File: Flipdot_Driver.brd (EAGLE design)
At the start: 146 x 75.9 mm, 27 parts

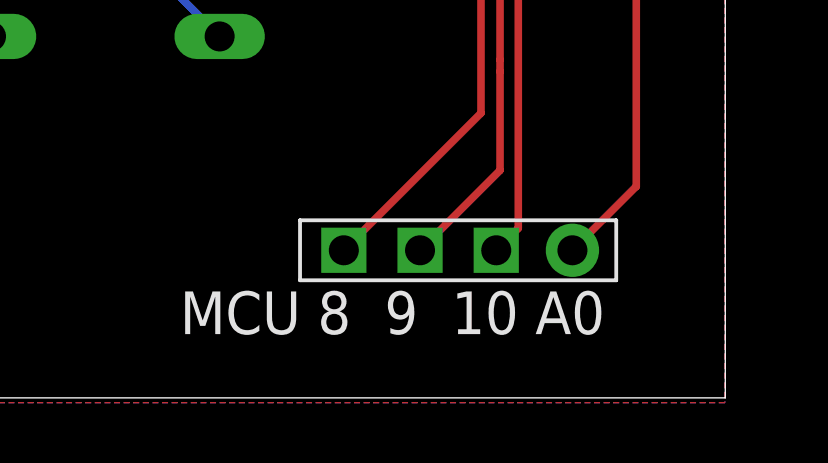
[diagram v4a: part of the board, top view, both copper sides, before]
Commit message: Remapped outputs, replaced MCU
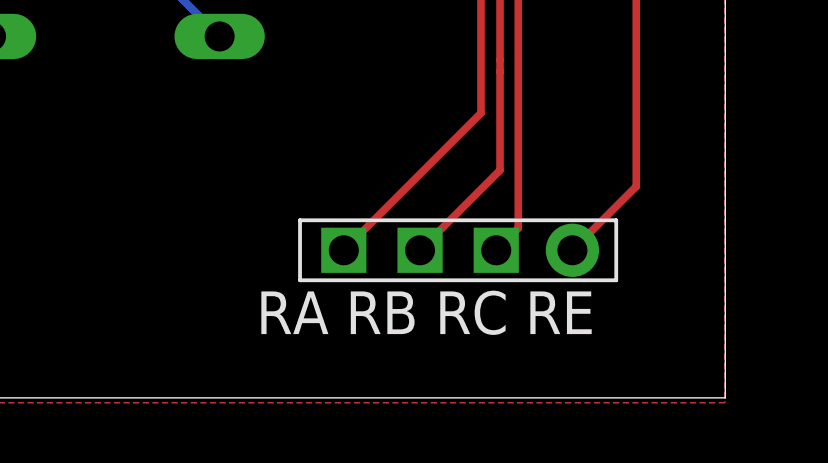
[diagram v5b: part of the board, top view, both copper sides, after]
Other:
- board text added: "A B C"
- board text added: "EA EB EC"
- board text added: "RA RB RC RE"
- board text removed: "MCU 2 3 4"
- board text removed: "MCU 5 6 7"
- board text removed: "MCU 8 9 10 A0"
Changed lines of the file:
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@@
 <?xml version="1.0" encoding="utf-8"?>
 <!DOCTYPE eagle SYSTEM "eagle.dtd">
-<eagle version="9.2.2">
+<eagle version="9.3.2">
 <drawing>
 <settings>
@@
 <wire x1="0.035" y1="76.03" x2="0.035" y2="0.16" width="0" layer="20"/>
 <text x="113.665" y="68.58" size="1.4224" layer="51">GND  5V  10V</text>
-<text x="18.161" y="2.921" size="1.4224" layer="51" rot="R90">MCU 2  3  4</text>
-<text x="2.54" y="52.07" size="1.4224" layer="51">MCU 5  6  7</text>
+<text x="13.081" y="8.001" size="1.4224" layer="51" rot="R90">A  B  C</text>
+<text x="2.159" y="51.943" size="1.4224" layer="51">EA EB EC</text>
 <text x="26.543" y="37.592" size="1.778" layer="51">The cake is a lie.</text>
-<text x="127.889" y="2.286" size="1.4224" layer="25">MCU 8  9  10 A0</text>
+<text x="130.429" y="2.286" size="1.4224" layer="25">RA RB RC RE</text>
 <text x="11.049" y="69.85" size="1.4224" layer="25">Seg. Sel.</text>
 </plain>

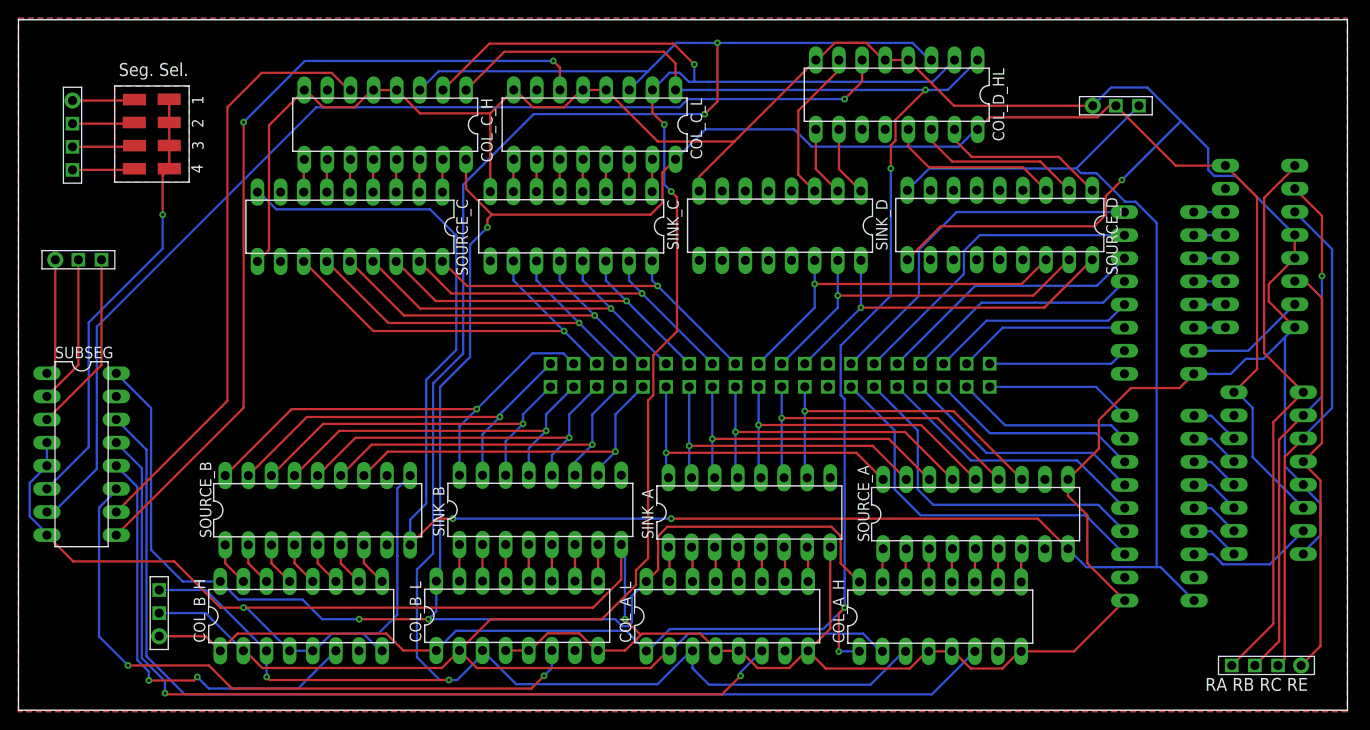
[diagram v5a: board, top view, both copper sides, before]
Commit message: Smaller PCB design
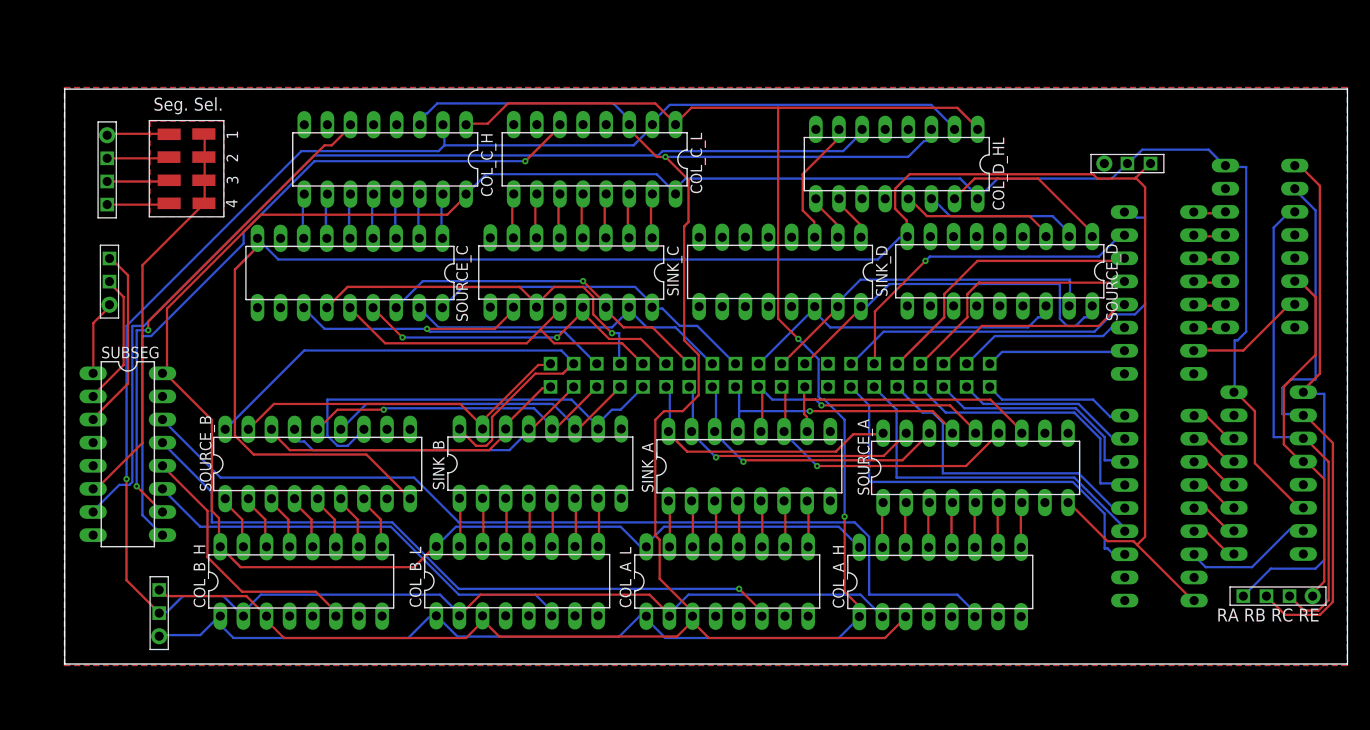
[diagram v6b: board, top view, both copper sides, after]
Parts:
- moved U$6 7.73 mm to (139.7, 12.7)
- moved COL_D_HL 7.62 mm to (96.5, 60.2)
- moved U$5 6.48 mm to (121.9, 60.2)
- moved U$10 5.39 mm to (18.5, 59.7)
- moved U$11 5.39 mm to (9.78, 60.8)
- moved SINK_A 5.08 mm to (80.3, 27.0)
- moved SINK_B 5.08 mm to (57.4, 27.3)
- moved SOURCE_B 5.08 mm to (32.9, 27.2)
- moved SUBSEG 5.08 mm to (12.0, 28.3)
- moved SINK_C 5.08 mm to (60.8, 48.3)
- moved SINK_D 5.08 mm to (83.7, 48.3)
- moved SOURCE_A 5.08 mm to (105.2, 26.8)
- moved SOURCE_C 5.08 mm to (36.5, 48.2)
- moved SOURCE_D 5.08 mm to (107.9, 48.4)
- moved U$3 4.18 mm to (10.0, 47.3), turned to 90 degrees
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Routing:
- net GND: track 519.3 -> 0.00 mm, vias 3 -> 0
- net C: track 255.4 -> 211.0 mm, vias 4 -> 1
- net 5V: track 305.1 -> 278.8 mm, vias 3 -> 0
- net N$10: track 72.0 -> 48.9 mm, vias 2 -> 0
- net N$7: track 97.6 -> 76.0 mm, vias 2 -> 1
- net N$9: track 122.1 -> 102.2 mm
- net N$8: track 48.0 -> 29.2 mm, vias 2 -> 0
- net 10V: track 229.4 -> 213.2 mm, vias 2 -> 0
- net N$12: track 91.5 -> 79.2 mm, vias 2 -> 1
- net N$11: track 65.4 -> 54.9 mm, vias 0 -> 2
- net C22: track 52.4 -> 61.2 mm, vias 1 -> 0
- net N$13: track 120.7 -> 112.2 mm, vias 1 -> 0
- net B: track 233.7 -> 226.1 mm, vias 3 -> 1
- net C15: track 40.5 -> 47.7 mm, vias 1 -> 0
- net R1L: track 39.9 -> 47.1 mm
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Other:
- board size 146 x 75.9 mm -> 140.9 x 63.2 mm
